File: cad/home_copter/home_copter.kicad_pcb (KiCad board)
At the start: 2 copper layers, 41.9 x 38.7 mm, 63 parts, among them U1 ICM-42670-P, U10 2pin_header, U11 2pin_header, U12 RQ5E040AJTCL, U13 RQ5E040AJTCL, U14 2pin_header, U15 2pin_header, U16 2pin_header, U17 2pin_header, U2 ESP32-C3-MINI-1-H4X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

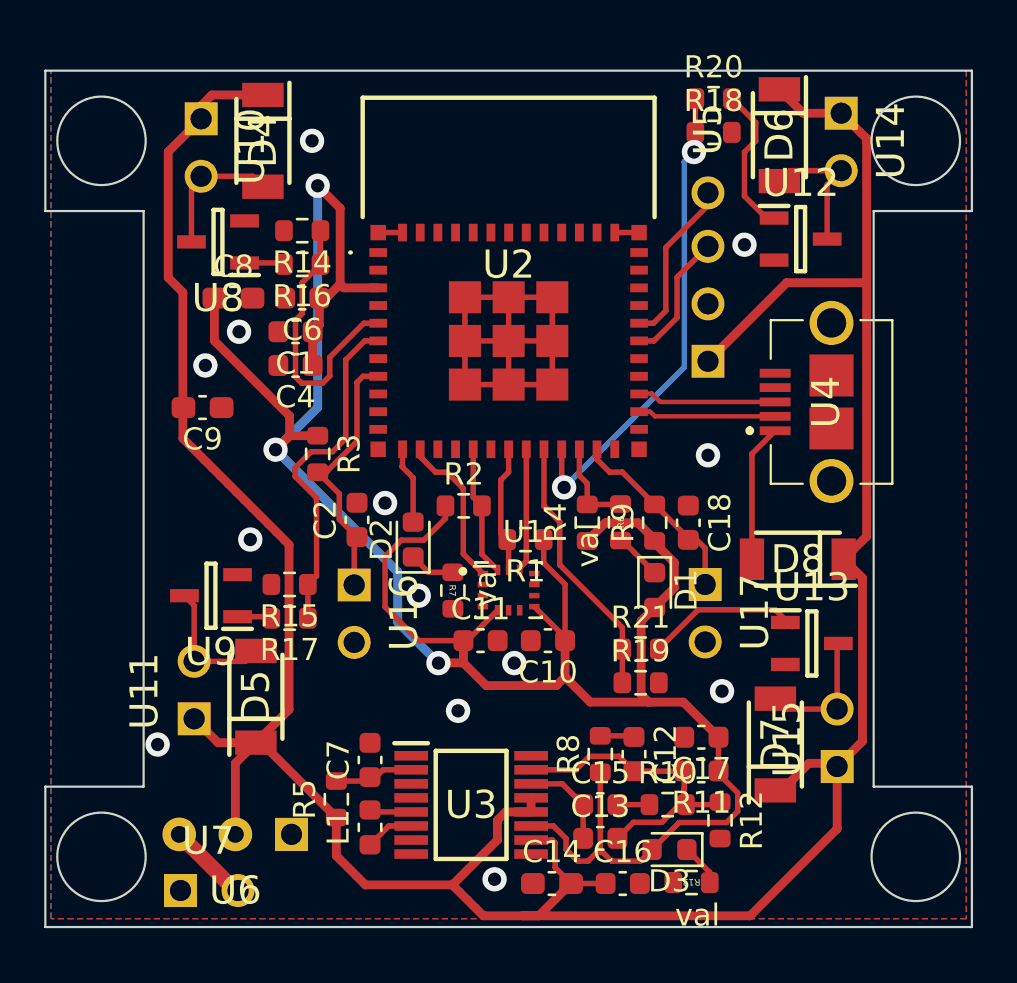
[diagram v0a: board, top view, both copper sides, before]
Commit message: Likely hand solderable copter pcb finally designed!
Signed-off-by: Andrew Wock <ajwock@gmail.com>
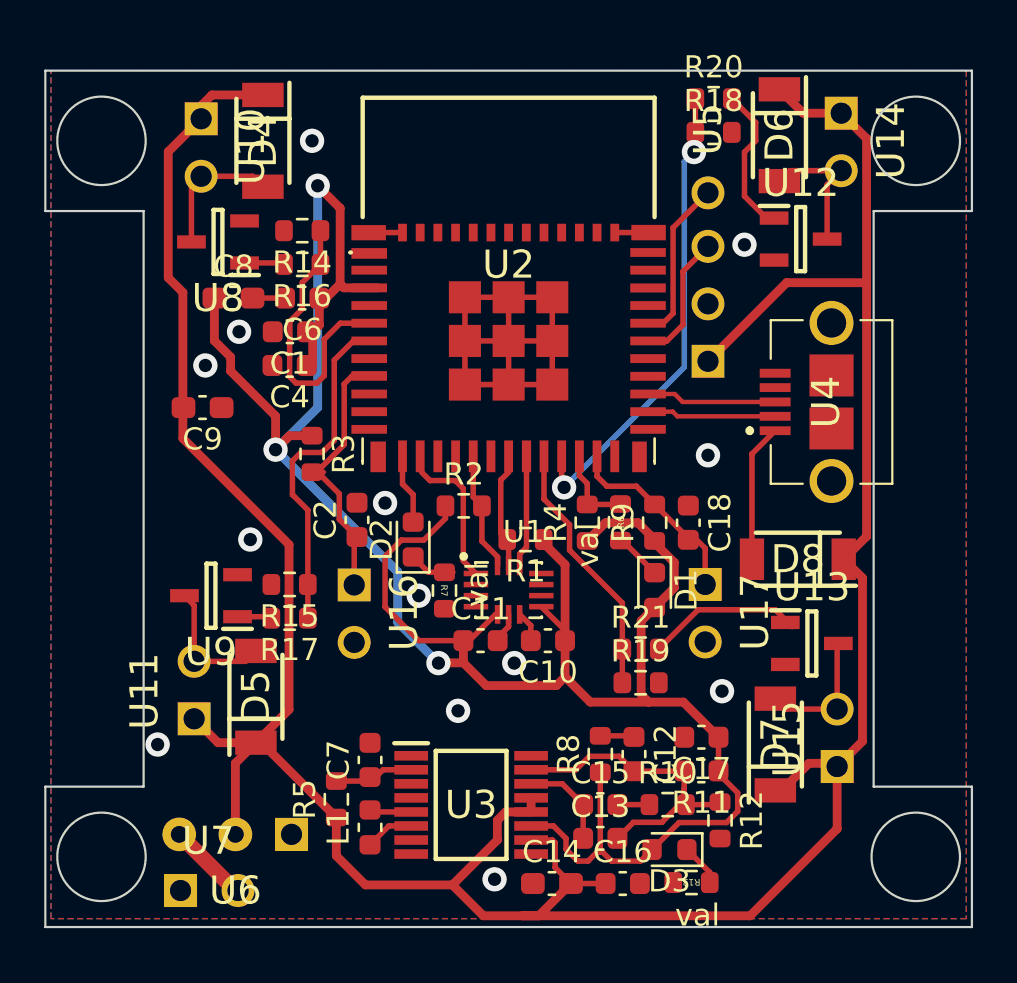
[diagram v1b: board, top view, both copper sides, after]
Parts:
- U1: footprint Rust_Board:IC_ICM-42670-P -> Imported:ICM-42670-hand-solder
- U2: footprint Imported:ESP32C3MINI1H4X -> Imported:ESP32C3MINI1H4X_hand_solder
- moved R7 0.38 mm to (30.7, 36.2)
- moved C4 0.27 mm to (23.7, 26.0)
- moved C1 0.25 mm to (23.8, 24.5)
- moved R3 0.25 mm to (24.8, 30.0)
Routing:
- net GND: track 25.9 -> 30.2 mm
- net UART_TX: track 6.82 -> 8.07 mm
- net pwm_frontleft: track 12.6 -> 13.6 mm
- net UART_RX: track 5.96 -> 6.57 mm
- net IO9_BOOT: track 8.50 -> 9.09 mm
